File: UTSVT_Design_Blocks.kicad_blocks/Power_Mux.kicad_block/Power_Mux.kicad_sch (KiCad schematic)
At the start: 8 parts, among them U1 TPS2117DRLR

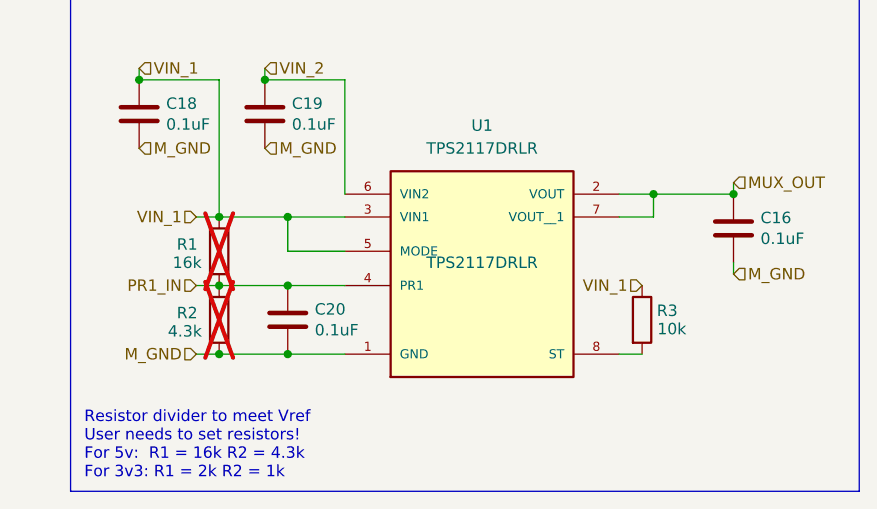
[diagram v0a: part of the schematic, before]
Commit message: changed ST to MuxOut pullup, adjusted load cap, fixed PN, removed default res values
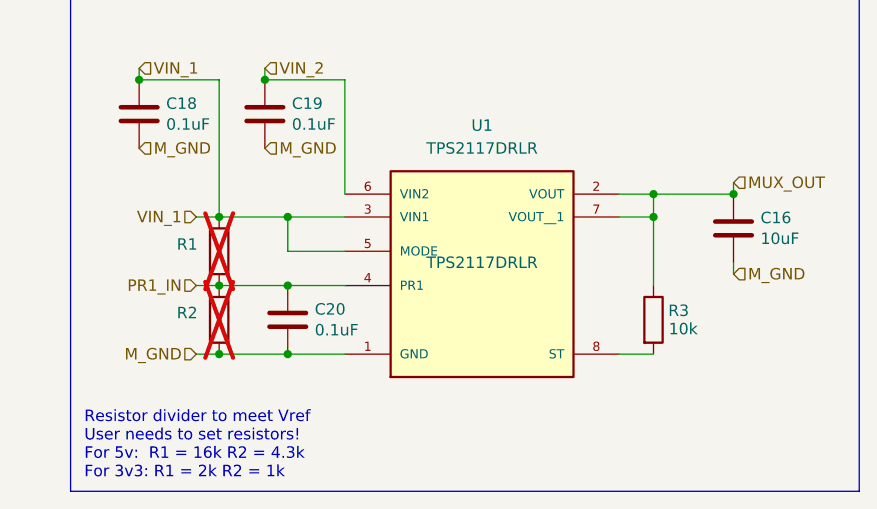
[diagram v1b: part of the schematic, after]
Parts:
- C16: value 0.1uF -> 10uF; P/N MLASH168SB7104KTNA01 -> GRM21BR61H106KE43K
- R1, R2: P/N CRCW060310K0FKEI -> (none)
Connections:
- net MUX_OUT: now also R3.1
- net VIN_1: no longer R3.1
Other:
- moved on the sheet: R3
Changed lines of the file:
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@@
+	)
+	(junction
+		(at 90.17 63.5)
+		(diameter 0)
+		(color 0 0 0 0)
 	)
 	(junction
@@
 	(wire
 		(pts
-			(xy 86.36 78.74) (xy 88.9 78.74)
+			(xy 86.36 78.74) (xy 90.17 78.74)
 		)
 		(stroke
@@
 		(pts
 			(xy 39.37 71.12) (xy 41.91 71.12)
+		)
+		(stroke
+			(width 0)
+			(type default)
+		)
+	)
+	(wire
+		(pts
+			(xy 90.17 63.5) (xy 90.17 71.12)
 		)
 		(stroke
@@
 		(shape input)
 		(at 39.37 71.12 180)
-		(effects
-			(font
-				(size 1.27 1.27)
-			)
-			(justify right)
-		)
-	)
-	(hierarchical_label "VIN_1"
-		(shape input)
-		(at 88.9 71.12 180)
 		(effects
 			(font
@@
 			)
 		)
-		(property "Value" "0.1uF"
+		(property "Value" "10uF"
 			(at 102.0572 65.913 0)
 			(effects
@@
 			)
 		)
-		(property "P/N" "MLASH168SB7104KTNA01"
+		(property "P/N" "GRM21BR61H106KE43K"
 			(at 99.06 64.77 0)
 			(effects
@@
 					(size 1.27 1.27)
 				)
+				(hide yes)
 			)
 		)
@@
 			)
 		)
-		(property "P/N" "CRCW060310K0FKEI "
+		(property "P/N" ""
 			(at 41.91 67.31 90)
 			(effects
@@
 	(symbol
 		(lib_id "Device:R")
-		(at 88.9 74.93 0)
+		(at 90.17 74.93 0)
 		(unit 1)
 		(exclude_from_sim no)
@@
 		(dnp no)
 		(property "Reference" "R3"
-			(at 91.694 73.914 0)
+			(at 92.964 73.914 0)
 			(effects
 				(font
@@
 		)
 		(property "Value" "10k"
-			(at 92.202 75.946 0)
+			(at 93.472 75.946 0)
 			(effects
 				(font
@@
 		)
 		(property "Footprint" "Resistor_SMD:R_0603_1608Metric_Pad0.98x0.95mm_HandSolder"
-			(at 87.122 74.93 90)
+			(at 88.392 74.93 90)
 			(effects
 				(font
@@
 		)
 		(property "Datasheet" "~"
-			(at 88.9 74.93 0)
+			(at 90.17 74.93 0)
 			(effects
 				(font
@@
 		)
 		(property "Description" "Resistor"
-			(at 88.9 74.93 0)
+			(at 90.17 74.93 0)
 			(effects
 				(font
@@
 		)
 		(property "P/N" "CRCW060310K0FKEI "
-			(at 88.9 74.93 90)
+			(at 90.17 74.93 90)
 			(effects
 				(font
@@
 					(size 1.27 1.27)
 				)
+				(hide yes)
 			)
 		)
@@
 			)
 		)
-		(property "P/N" "CRCW060310K0FKEI "
+		(property "P/N" ""
 			(at 41.91 74.93 90)
 			(effects

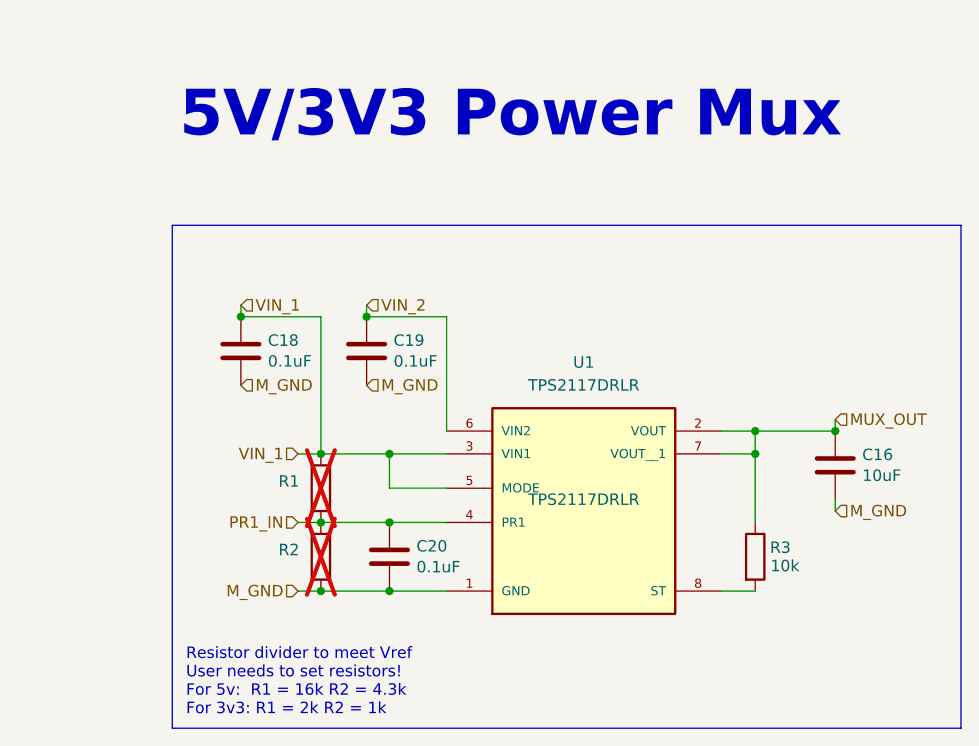
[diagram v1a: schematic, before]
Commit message: added info about input range. changed to have power symbols & one heirarchical label. mentioned automatic mode config. muxout is now an output
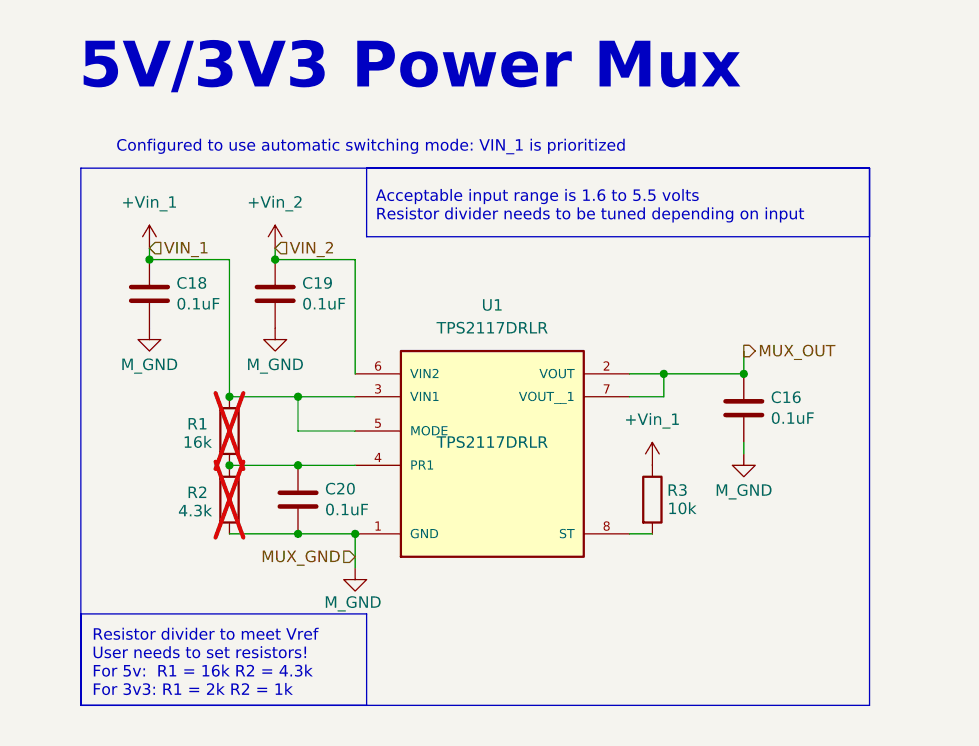
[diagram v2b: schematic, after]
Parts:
- C16: value 10uF -> 0.1uF; P/N GRM21BR61H106KE43K -> MLASH168SB7104KTNA01
- R1, R2: P/N (none) -> CRCW060310K0FKEI
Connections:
- net MUX_OUT: no longer R3.1
- net PR1_IN: no longer names the net of C20.1, R1.2, R2.1, U1.4 (PR1)
- net VIN_1 renamed +Vin_1
- net +Vin_1: now also R3.1
- net VIN_2 renamed +Vin_2
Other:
- note added: "Acceptable input range is 1.6 to 5.5 volts Resistor divider needs to be tuned depending on input"
- note added: "Configured to use automatic switching mode: VIN_1 is prioritized"
- moved on the sheet: C16, C18, C19, C20, R1, R2, R3, U1

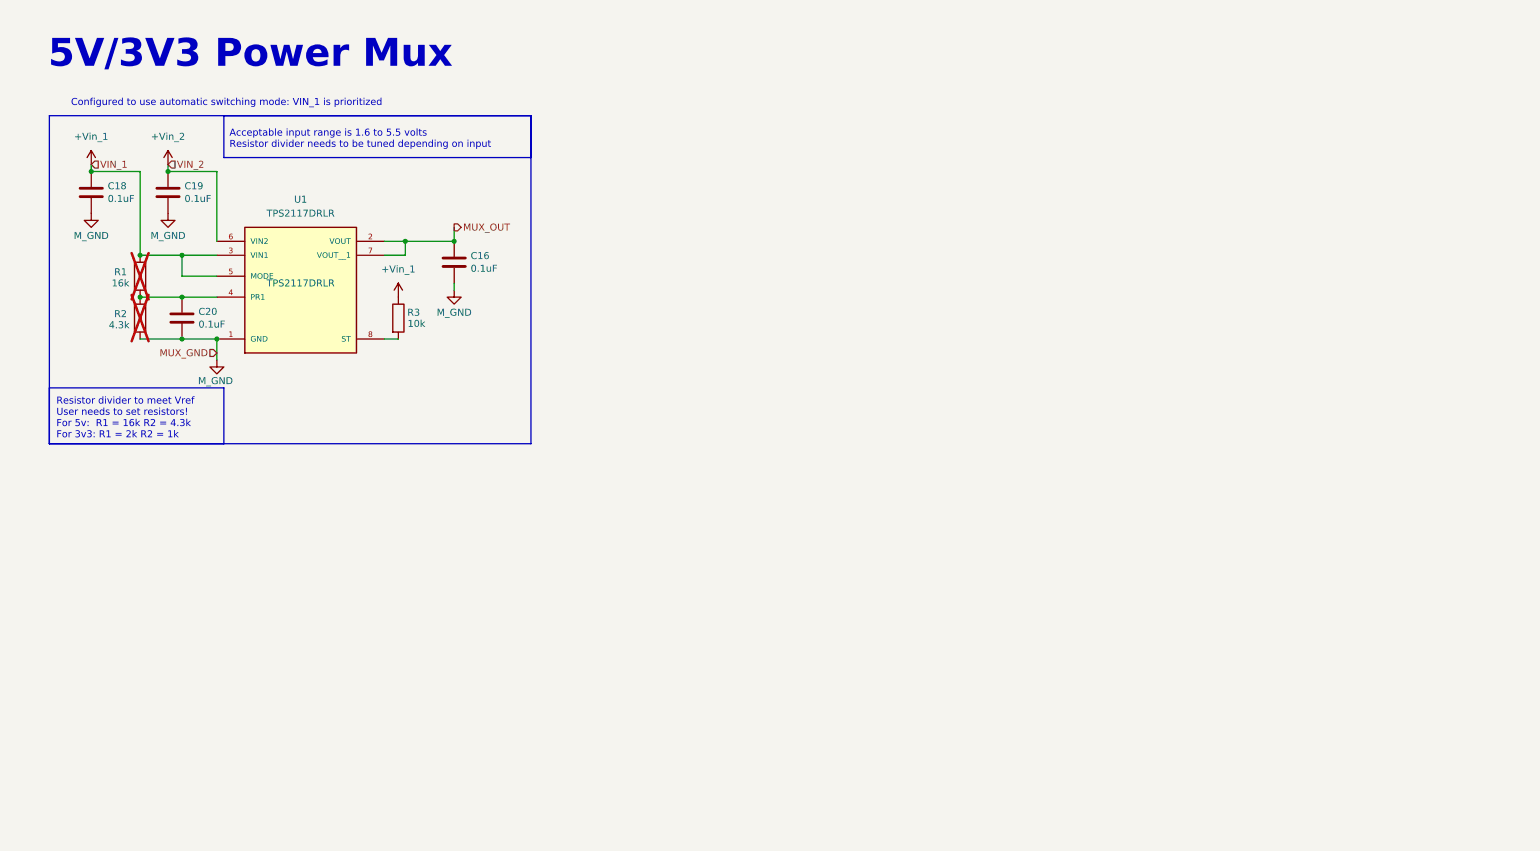
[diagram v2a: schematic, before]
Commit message: lowered max thresholds for switching, embedded datasheet into symbol
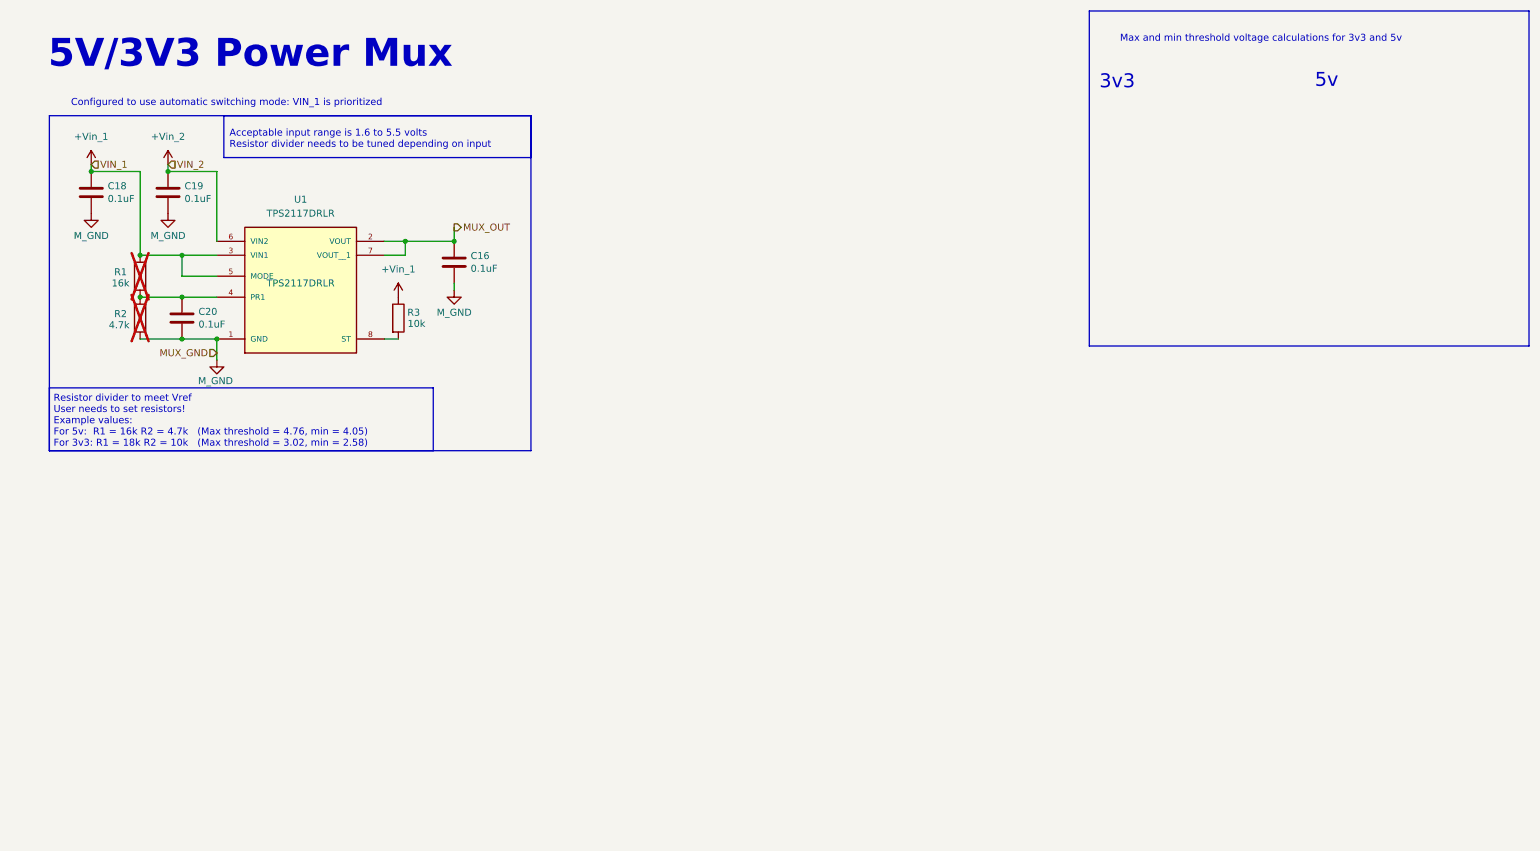
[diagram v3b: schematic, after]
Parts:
- R2: value 4.3k -> 4.7k
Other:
- note added: "3v3"
- note added: "5v"
- note added: "Max and min threshold voltage calculations for 3v3 and 5v"
- note added: "Resistor divider to meet Vref User needs to set resistors! Example values: For 5v: R1 = 16k R2 = 4.7k (Max threshold = 4.76, min = 4.05) For 3v3: R1 = 18k R2 = 10k (Max threshold = 3.02, min = 2.58)"
- note removed: "Resistor divider to meet Vref User needs to set resistors! For 5v: R1 = 16k R2 = 4.3k For 3v3: R1 = 2k R2 = 1k"

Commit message: only uses hierarchical labels now, seperate symbol library
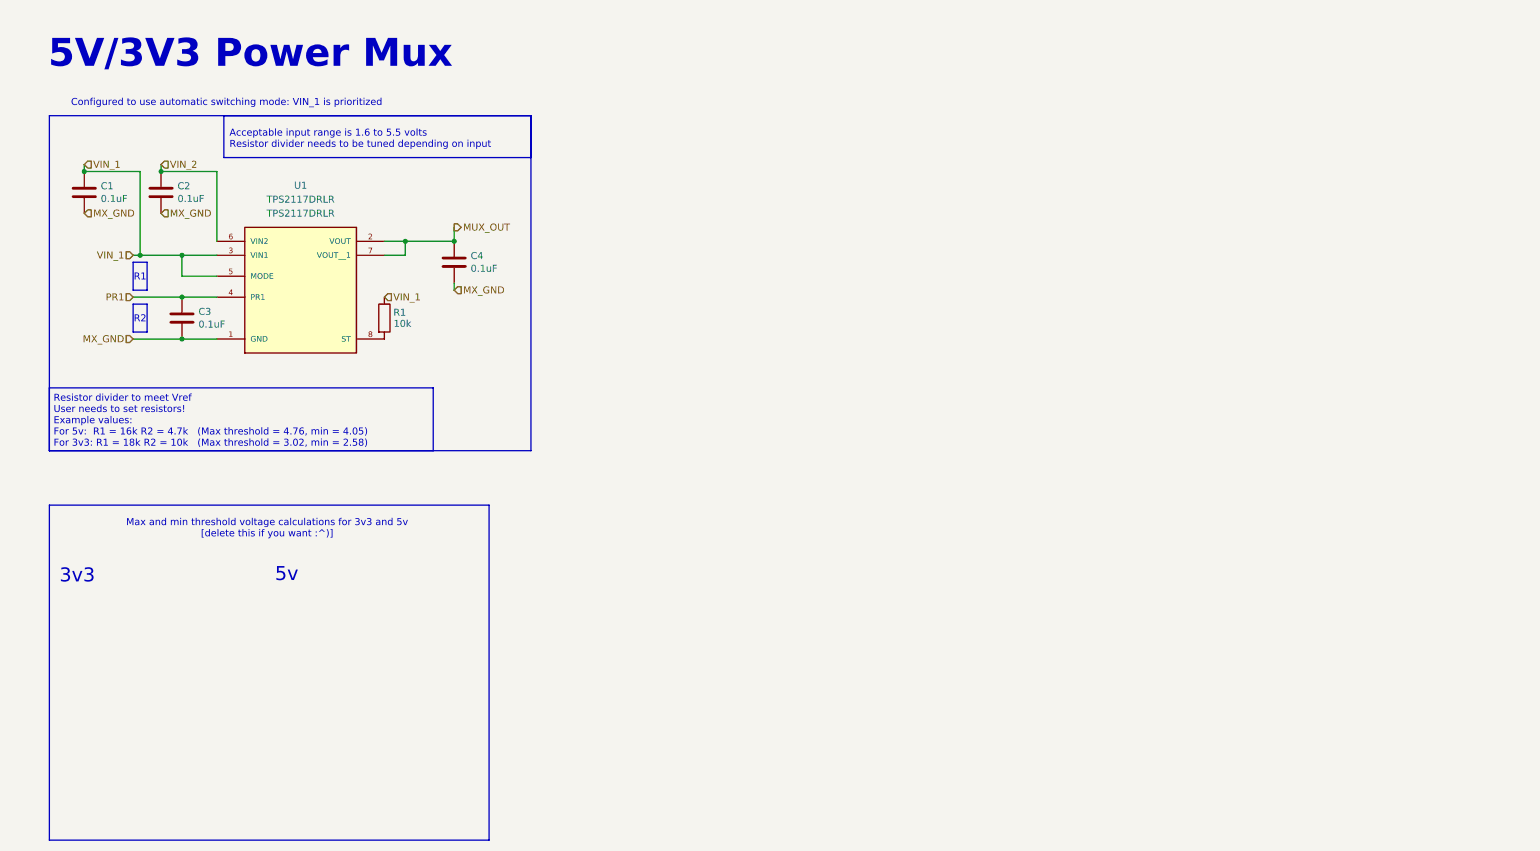
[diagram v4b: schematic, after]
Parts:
- removed R1: 16k, Resistor_SMD:R_0603_1608Metric_Pad0.98x0.95mm_HandSolder, symbol Device:R
- removed R2: 4.7k, Resistor_SMD:R_0603_1608Metric_Pad0.98x0.95mm_HandSolder, symbol Device:R
- removed U1: TPS2117DRLR, UTSVT_ICs:TPS2117DRLR, symbol TPS2117DRLR:TPS2117DRLR
- added U1: TPS2117DRLR, pretty:TPS2117DRLR, symbol mux:TPS2117DRLR
- renumbered C18 to C1, C19 to C2, C20 to C3, C16 to C4, R3 to R1
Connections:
- net MUX_OUT: now also U1.2 (VOUT), U1.7 (VOUT__1)
- net PR1: now reaches C3.1
- net PR1: now also U1.4 (PR1)
- net at R1.2: now also U1.8 (ST)
- net +Vin_1 renamed VIN_1
- net VIN_1: now also U1.3 (VIN1), U1.5 (MODE)
- net +Vin_2 renamed VIN_2
- net VIN_2: now also U1.6 (VIN2)
- net M_GND renamed MX_GND
- net MX_GND: now also U1.1 (GND)
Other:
- note added: "Max and min threshold voltage calculations for 3v3 and 5v [delete this if you want :^)]"
- note added: "R1"
- note added: "R2"
- note removed: "Max and min threshold voltage calculations for 3v3 and 5v"
- moved on the sheet: C1, C2, R1
